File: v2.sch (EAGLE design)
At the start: 42 parts, among them Q1 12MHz

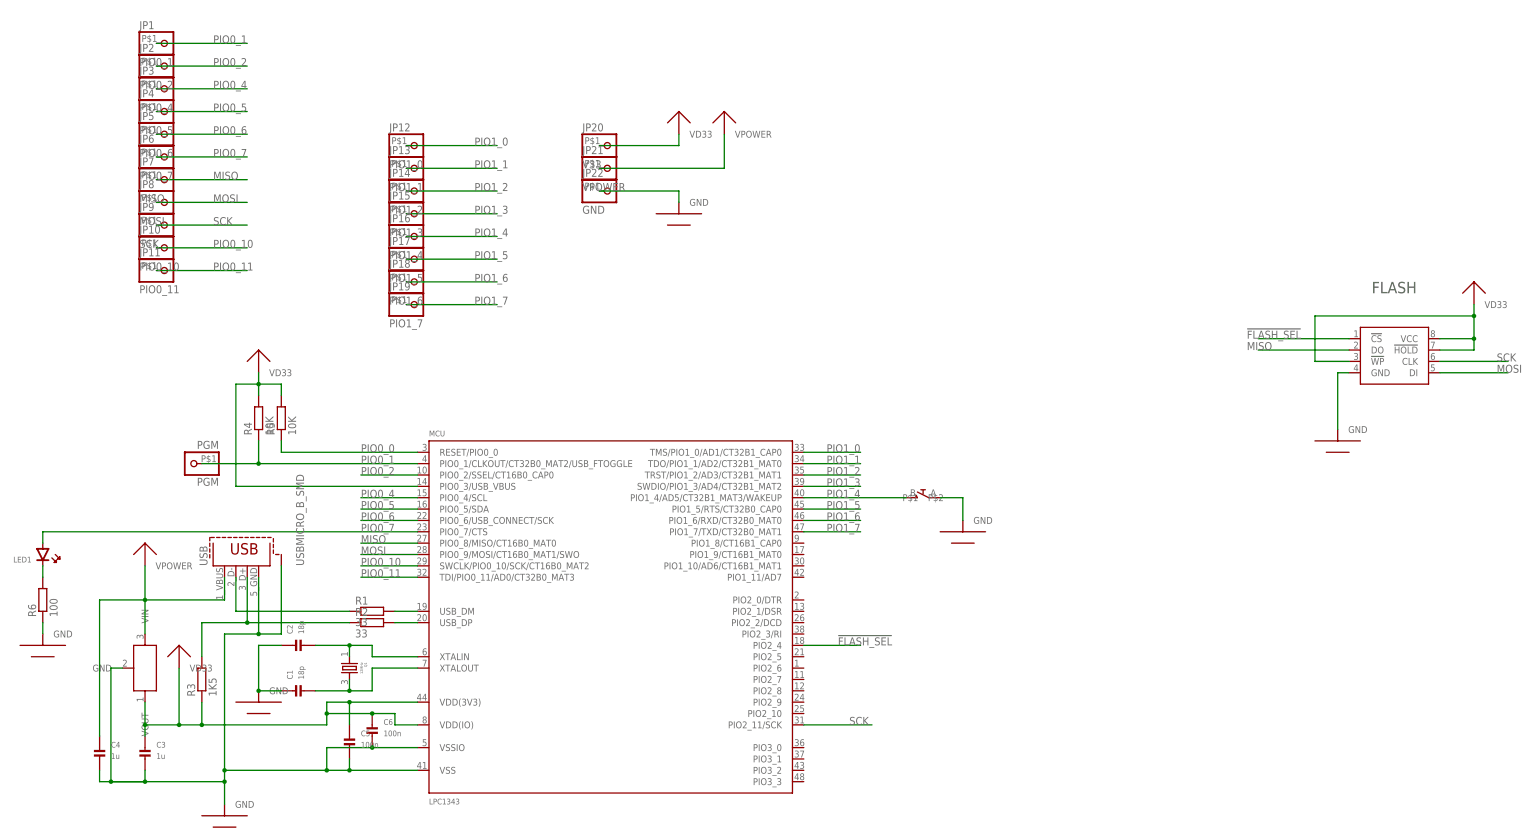
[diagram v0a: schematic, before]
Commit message: changed voltage regulator, routed more pins
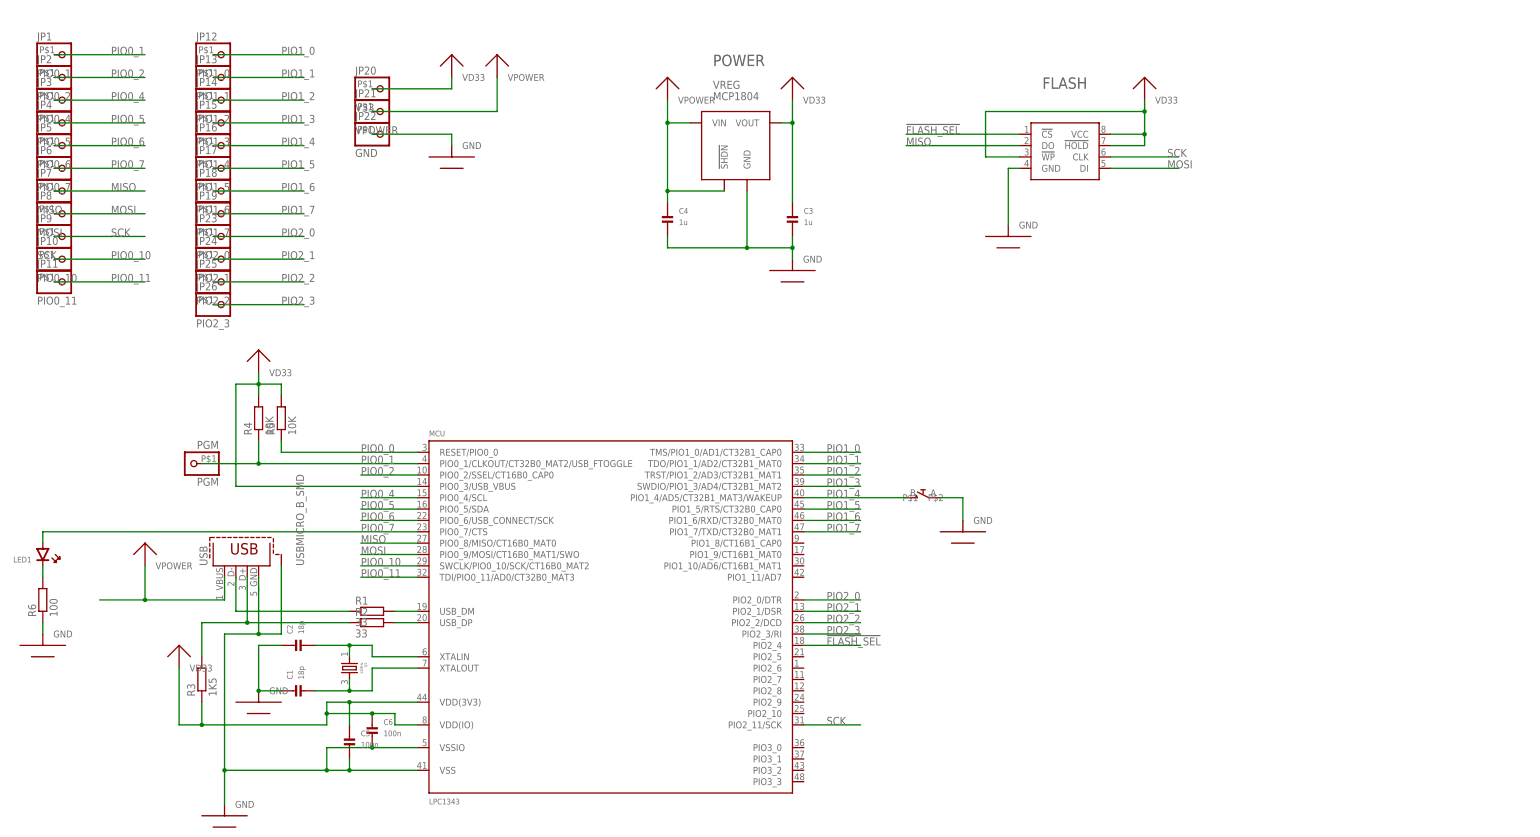
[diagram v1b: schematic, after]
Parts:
- added JP23: PIO2_0, MEINZEUG:HEADER-1X1SMD_MEDIUM
- added JP24: PIO2_1, MEINZEUG:HEADER-1X1SMD_MEDIUM
- added JP25: PIO2_2, MEINZEUG:HEADER-1X1SMD_MEDIUM
- added JP26: PIO2_3, MEINZEUG:HEADER-1X1SMD_MEDIUM
- VREG: device MEINZEUG:L78LSOT89-3 -> MEINZEUG:MCP180XSOT-23-5
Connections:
- new net PIO2_0: JP23.1, MCU.PIO2_0/DTR
- new net PIO2_1: JP24.1, MCU.PIO2_1/DSR
- new net PIO2_2: JP25.1, MCU.PIO2_2/DCD
- new net PIO2_3: JP26.1, MCU.PIO2_3/RI
- net VPOWER: now also VREG.!SHDN
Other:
- note added: "POWER"
- moved on the sheet: C3, C4, JP1, JP10, JP11, JP12, JP13, JP14, JP15, JP16, JP17, JP18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

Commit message: vreg label 1801
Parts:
- VREG: value MCP1804 -> MCP1801
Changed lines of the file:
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@@
 <parts>
 <part name="MCU" library="MEINZEUG" deviceset="LPC1343_QFP" device="" value="LPC1343"/>
-<part name="VREG" library="MEINZEUG" deviceset="MCP180X" device="SOT-23-5" value="MCP1804"/>
+<part name="VREG" library="MEINZEUG" deviceset="MCP180X" device="SOT-23-5" value="MCP1801"/>
 <part name="Q1" library="MEINZEUG" deviceset="QUARTZ" device="ABM8G" value="12MHz"/>
 <part name="C1" library="MEINZEUG" deviceset="CAP_CERAMIC" device="0805_MICROMELF_COMBO" value="18p"/>

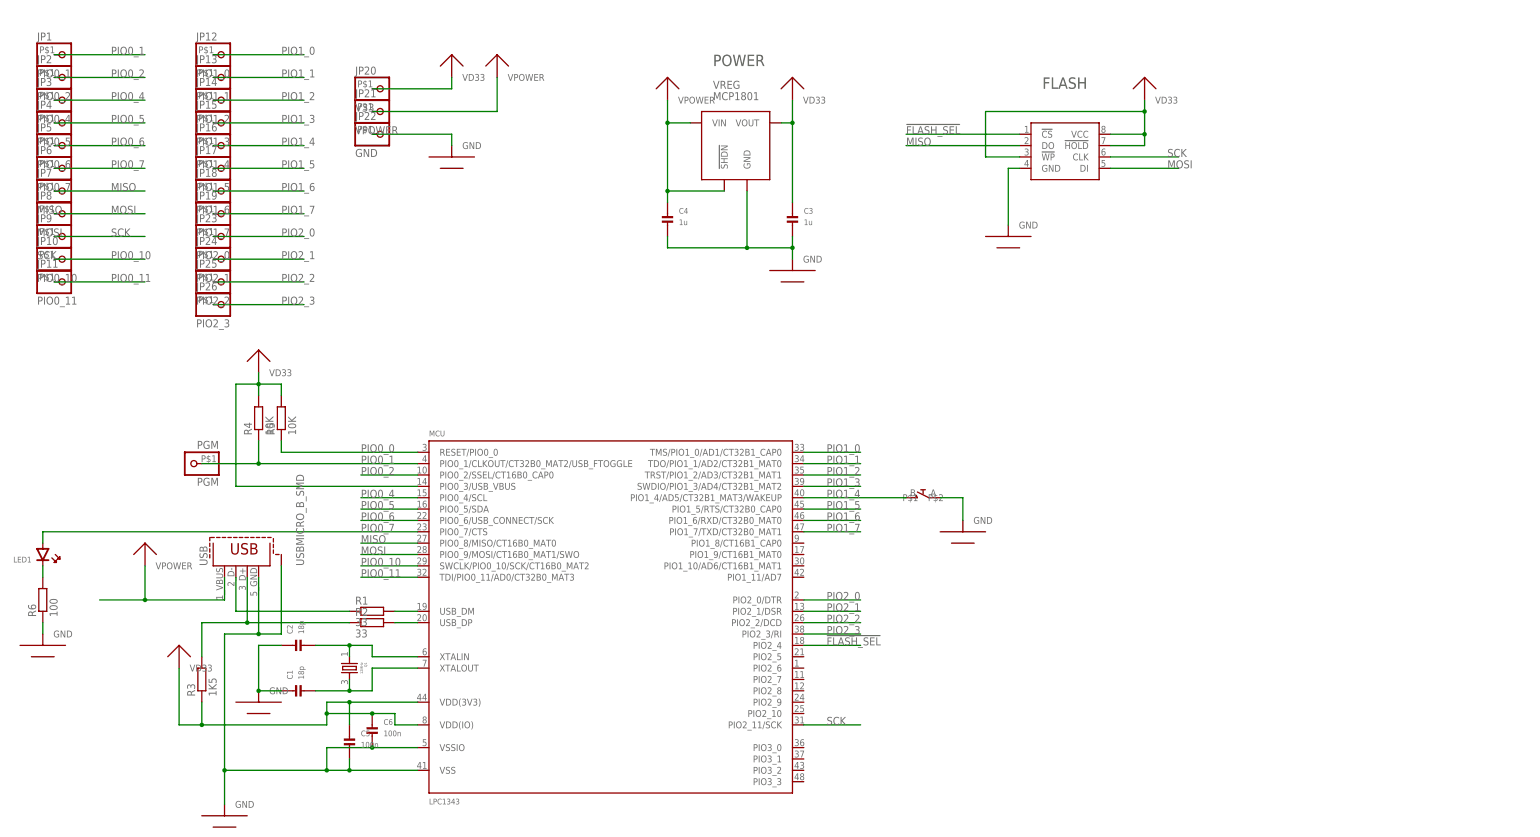
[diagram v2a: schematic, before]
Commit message: Added softconnect transistor, vast cleanup
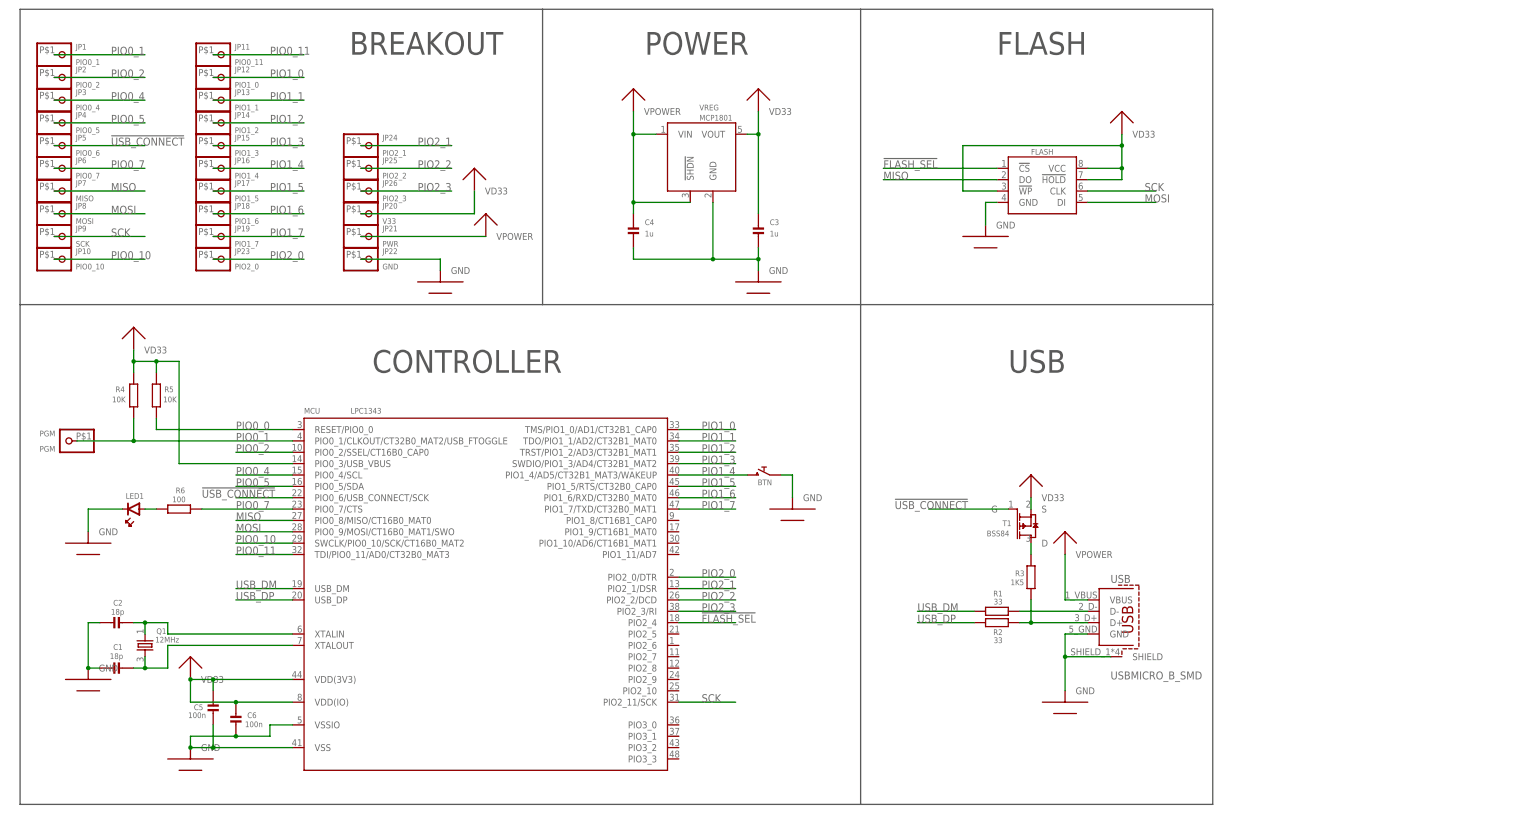
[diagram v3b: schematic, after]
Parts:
- added T1: BSS84, MEINZEUG:PMOS_ENH
- JP21: value VPOWER -> PWR
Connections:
- net N$4 renamed USB_DM
- net N$6 renamed USB_DP
- removed net PIO0_6: JP5.1, MCU.PIO0_6/USB_CONNECT/SCK
- removed net USB_D-: R1.1, USB.2
- new net !USB_CONNECT: JP5.1, MCU.PIO0_6/USB_CONNECT/SCK, T1.G
- new net N$3: R3.1, T1.D
- new net N$4: R1.1, USB.D-
- net GND: now also BTN.1, LED1.CATHODE, USB.GND; no longer BTN.P$1, R6.1, USB.4
- net N$5: now also LED1.ANODE, R6.1; no longer LED1.CATHODE, R6.2
- net PIO0_7: now also R6.2; no longer LED1.ANODE
- net PIO1_4: now also BTN.2; no longer BTN.P$2
- net USB_D+: now also USB.D+; no longer USB.3
- net VD33: now also T1.S; no longer R3.1
- net VPOWER: now also USB.VBUS; no longer USB.1
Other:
- note added: "BREAKOUT"
- note added: "CONTROLLER"
- note added: "USB"
- moved on the sheet: C1, C2, C3, C4, C5, C6, JP11, JP12, JP13, JP14, JP15, JP16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

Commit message: Board adjustments to comply with MakePCB.com
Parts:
- renumbered LED1 to LED
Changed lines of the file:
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@@
 <part name="U$8" library="MEINZEUG" deviceset="GND" device=""/>
 <part name="PGM" library="MEINZEUG" deviceset="HEADER-1X1" device="SMD_MEDIUM" value="PGM"/>
-<part name="LED1" library="MEINZEUG" deviceset="LED" device="0805" value=" "/>
+<part name="LED" library="MEINZEUG" deviceset="LED" device="0805" value=" "/>
 <part name="R6" library="MEINZEUG" deviceset="R-EU_" device="0805_MICROMELF_COMBO" value="100"/>
 <part name="U$6" library="MEINZEUG" deviceset="GND" device=""/>
@@
 <instance part="U$8" gate="G$1" x="55.88" y="43.18"/>
 <instance part="PGM" gate="G$1" x="-106.68" y="55.88" rot="R180"/>
-<instance part="LED1" gate="G$1" x="-91.44" y="40.64" smashed="yes" rot="R90">
+<instance part="LED" gate="G$1" x="-91.44" y="40.64" smashed="yes" rot="R90">
 <attribute name="NAME" x="-93.218" y="42.926" size="1.27" layer="95" font="vector"/>
 <attribute name="VALUE" x="-90.17" y="43.18" size="1.27" layer="96" font="vector" rot="R90"/>
@@
 </segment>
 <segment>
-<pinref part="LED1" gate="G$1" pin="CATHODE"/>
+<pinref part="LED" gate="G$1" pin="CATHODE"/>
 <wire x1="-93.98" y1="40.64" x2="-101.6" y2="40.64" width="0.1524" layer="91"/>
 <pinref part="U$6" gate="G$1" pin="GND"/>
@@
 <segment>
 <pinref part="R6" gate="G$1" pin="1"/>
-<pinref part="LED1" gate="G$1" pin="ANODE"/>
+<pinref part="LED" gate="G$1" pin="ANODE"/>
 <wire x1="-86.36" y1="40.64" x2="-88.9" y2="40.64" width="0.1524" layer="91"/>
 </segment>
